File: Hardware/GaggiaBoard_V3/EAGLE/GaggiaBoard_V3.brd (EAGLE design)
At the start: 45 x 100 mm, 68 parts, among them IC1 LD117AS33TR, J1 4PIN, J10 PIN262409-1, J11 PIN262409-1, J12 PIN262409-1, J13 PIN262409-1, J2 Vertical Qwiic Connector, J5 2PIN, J6 3PIN, J7 3PIN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

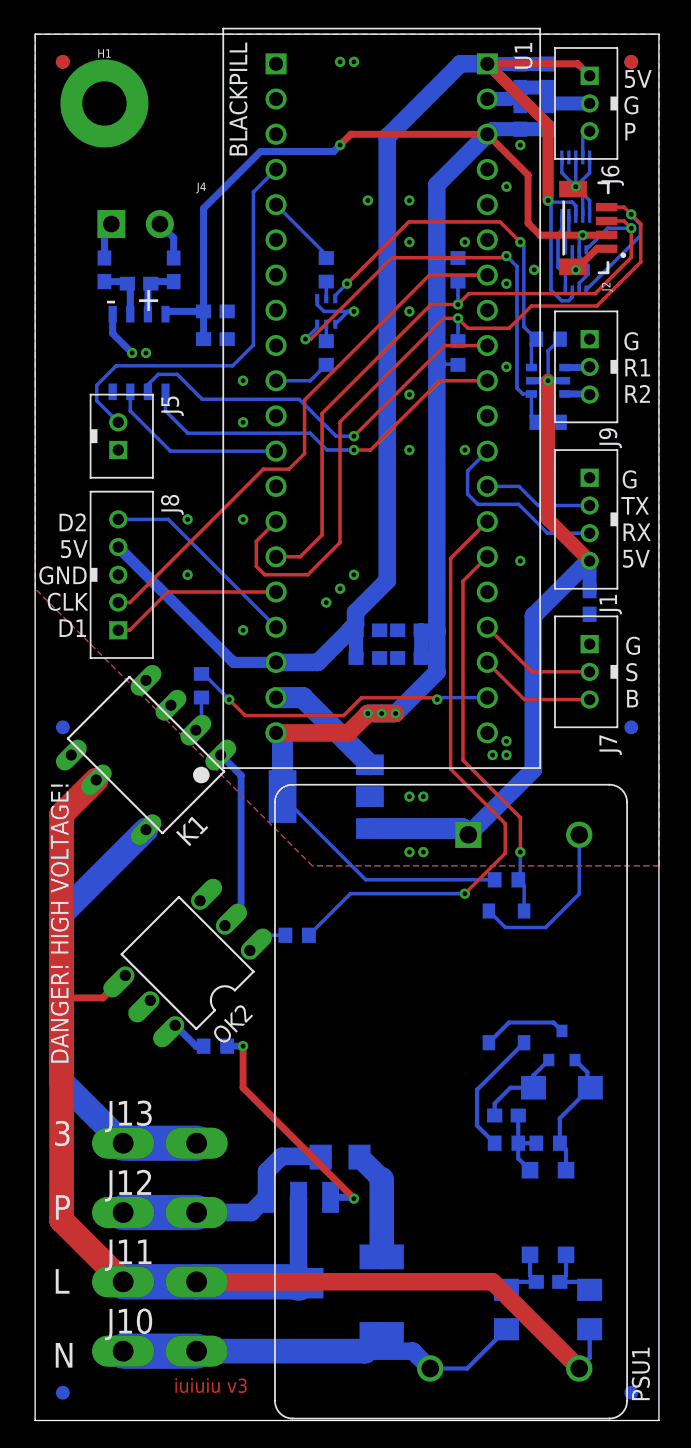
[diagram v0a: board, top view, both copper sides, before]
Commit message: UART added
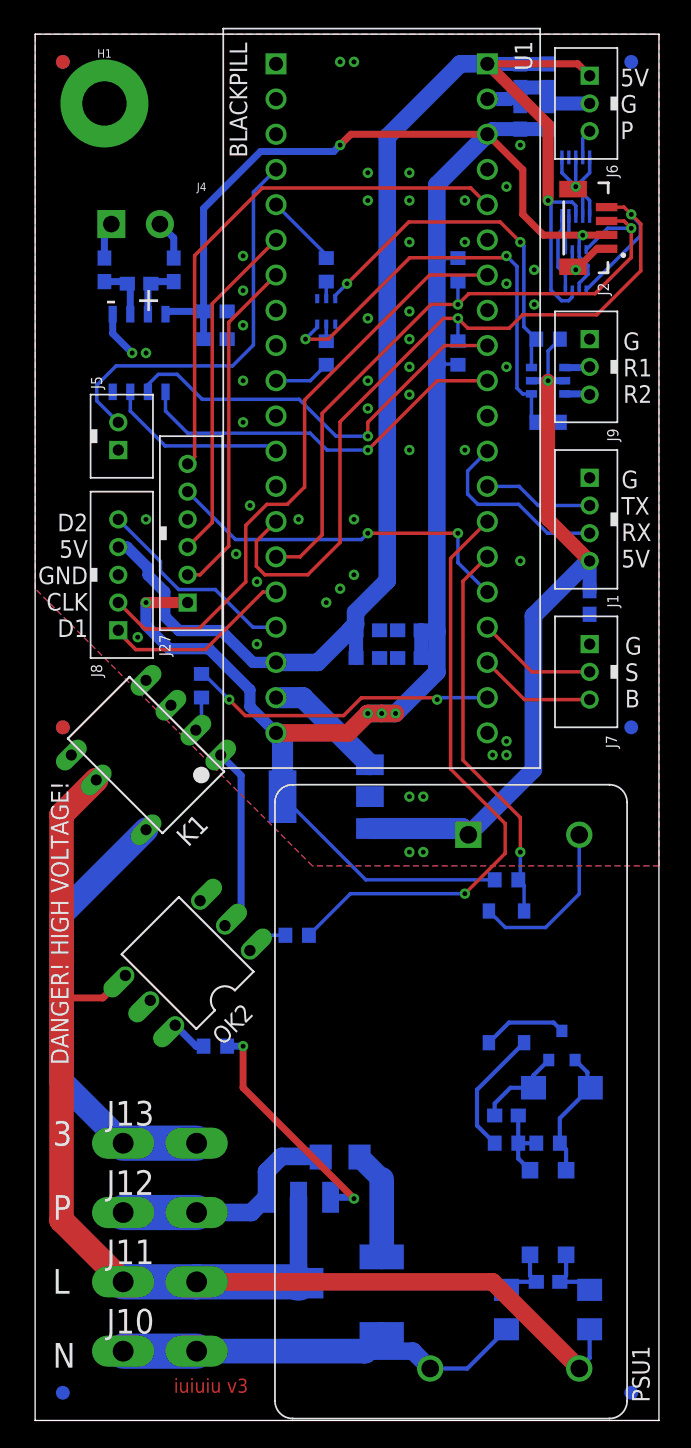
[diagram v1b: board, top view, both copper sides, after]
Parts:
- added J27: 6PIN, jst_eph:B6B-PH-K-S
- moved MARK8 63.1 mm to (2.00, 50.0)
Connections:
- net 3V3: now also J27.1
- net BOOT1: now also J27.6
- net GND: now also J27.4
- net NRST: now also J27.5
- net UART1_RX: now also J27.2
- net UART1_TX: now also J27.3
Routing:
- net BOOT1: track 0.00 -> 38.9 mm
- net NRST: track 0.00 -> 26.2 mm, vias 0 -> 2
- net UART1_TX: track 0.00 -> 24.8 mm
- net UART1_RX: track 0.00 -> 24.8 mm
- net 3V3: track 142.3 -> 160.1 mm, vias 5 -> 6
- net PB0: track 38.7 -> 44.0 mm
- net GND: track 69.7 -> 64.6 mm, vias 37 -> 52
- net 5V: track 161.6 -> 163.0 mm
- net PB8: track 12.5 -> 13.8 mm
- net PA6: track 29.9 -> 30.4 mm
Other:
- board text added: "BOOT1 NRST GND TX RX 3V3"

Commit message: README + PC13 load fix
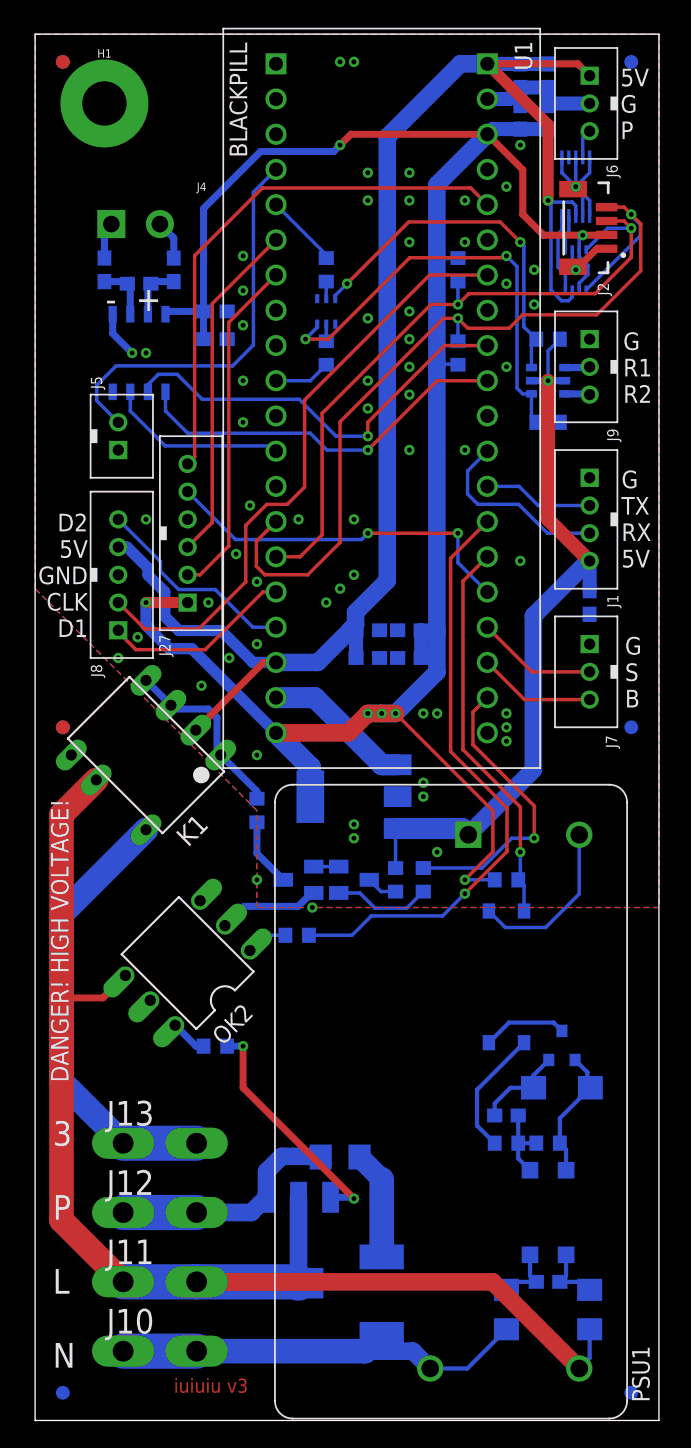
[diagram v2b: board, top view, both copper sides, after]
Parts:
- added R3, R4: 10K, rcl:R0603
- added T1, T2: (no value), transistor:SOT23-BEC
- R8: value 10K -> 220
- moved R8 9.85 mm to (16.0, 44.0), turned to 90 degrees
- moved IC1 2.00 mm to (23.0, 45.0)
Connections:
- new net N$11: R8.1, T2.C
- new net N$12: T1.E, T2.B
- new net N$13: K1.1, K1.3, K1.4, R8.2
- new net N$14: R4.2, T1.B
- net 5V: now also K1.2, R3.2
- net GND: now also T2.E; no longer K1.1, K1.3, K1.4
- net N$1: now also R3.1, T1.C; no longer K1.2, R8.2
- net PC13: now also R4.1; no longer R8.1
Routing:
- net N$13: track 0.00 -> 13.3 mm
- net 5V: track 163.0 -> 171.7 mm
- net N$14: track 0.00 -> 7.05 mm
- net N$11: track 0.00 -> 4.94 mm
- net GND: track 64.6 -> 60.6 mm, vias 52 -> 62
- net N$12: track 0.00 -> 1.80 mm
- net PC13: track 22.5 -> 21.3 mm, vias 2 -> 1
- net 3V3: track 160.1 -> 160.3 mm, vias 6 -> 7

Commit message: J1 fix
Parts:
- moved C4 9.49 mm to (37.0, 68.0), turned to 0 degrees
- moved FB2 2.50 mm to (3.50, 85.0)
- moved FB1 2.24 mm to (11.0, 85.0)
- moved C1 2.00 mm to (13.0, 82.0)
- moved C2 2.00 mm to (13.0, 80.0)
- moved C3 2.00 mm to (7.50, 84.0)
- moved U2 2.00 mm to (7.50, 79.0)
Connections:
- net 5V: now also J1.1; no longer J1.4
- net GND: now also J1.4; no longer J1.1
- net UART2_RX: now also J1.2; no longer J1.3
- net UART2_TX: now also J1.3; no longer J1.2
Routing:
- net UART2_RX: track 13.7 -> 9.00 mm
- net SPI1_SCK: track 27.8 -> 29.8 mm
- net SPI1_MISO: track 13.1 -> 15.1 mm
- net 3V3: track 160.3 -> 158.3 mm
- net N$5: track 4.00 -> 5.50 mm
- net N$26: track 4.00 -> 5.00 mm
- net 5V: track 171.7 -> 172.6 mm
- net UART2_TX: track 7.95 -> 8.78 mm
- net PB15: track 29.2 -> 30.0 mm
- net PA6: track 30.4 -> 31.2 mm
- net N$4: track 2.86 -> 2.19 mm
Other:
- board text added: "5V RX TX G"
- board text removed: "G TX RX 5V"

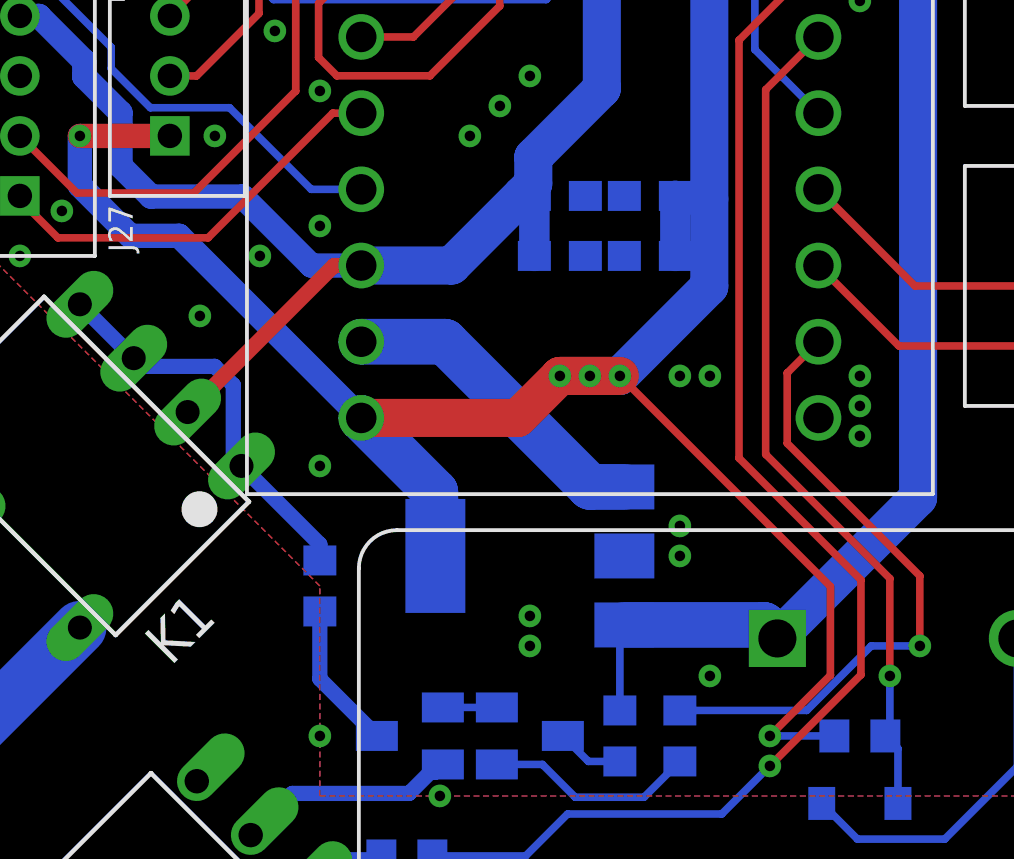
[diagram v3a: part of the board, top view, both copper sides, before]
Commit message: 5V supply fix
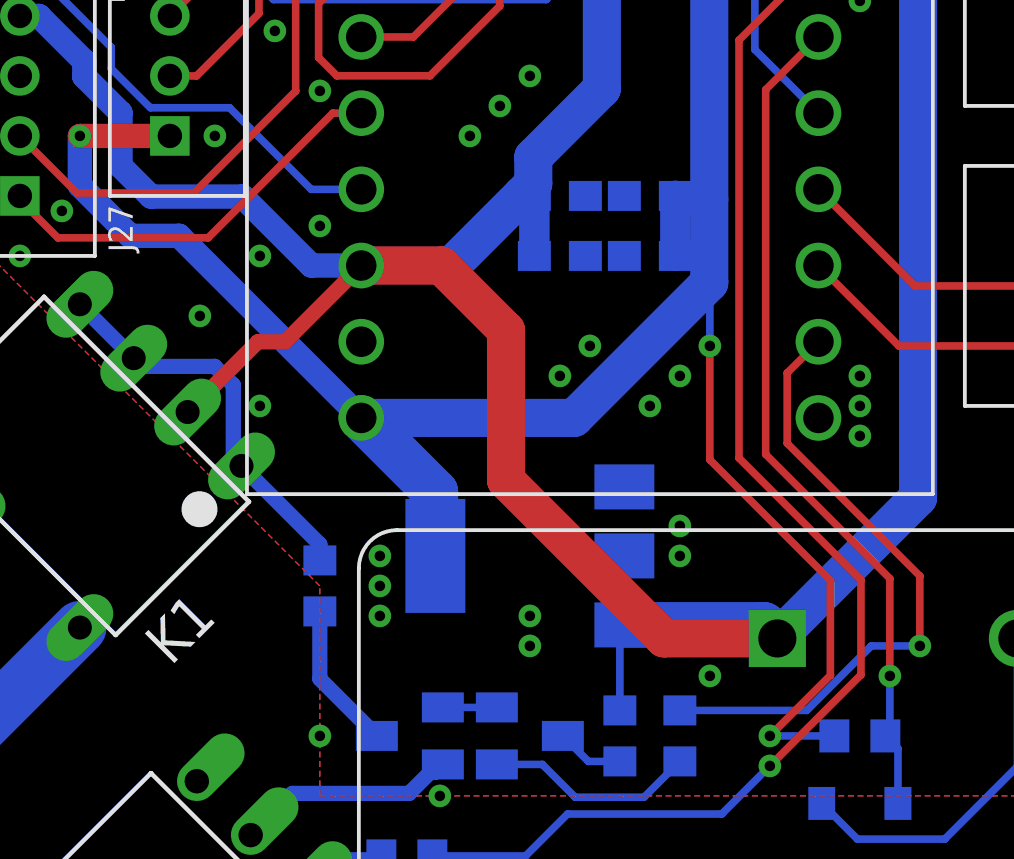
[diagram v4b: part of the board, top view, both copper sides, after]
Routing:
- net 5V: track 172.6 -> 194.6 mm
- net GND: track 60.6 -> 49.9 mm, vias 62 -> 67
- net 3V3: track 158.3 -> 158.1 mm, vias 7 -> 5
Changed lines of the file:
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@@
 <setting verticaltext="up"/>
 </settings>
-<grid distance="50" unitdist="mil" unit="mil" style="lines" multiple="1" display="no" altdistance="5" altunitdist="mil" altunit="mil"/>
+<grid distance="1" unitdist="mm" unit="mm" style="lines" multiple="1" display="no" altdistance="0.1" altunitdist="mm" altunit="mm"/>
 <layers>
 <layer number="1" name="Top" color="4" fill="1" visible="yes" active="yes"/>
@@
 <element name="T2" library="transistor" library_urn="urn:adsk.eagle:library:402" package="SOT23-BEC" package3d_urn="urn:adsk.eagle:package:28748/2" value="" x="19" y="39" smashed="yes" rot="MR270">
 <attribute name="LCSC" value="C82460" x="19" y="39" size="1.778" layer="28" rot="MR270" display="off"/>
-<attribute name="NAME" x="17.995" y="42.505" size="1.27" layer="26" rot="MR270"/>
+<attribute name="NAME" x="17.795" y="42.205" size="1.27" layer="26" rot="MR270"/>
 <attribute name="POPULARITY" value="0" x="19" y="39" size="1.778" layer="28" rot="MR270" display="off"/>
 <attribute name="VALUE" x="22.175" y="40.905" size="1.27" layer="28" rot="MR270"/>
@@
 <wire x1="38.75" y1="84.45" x2="38.75" y2="83.25" width="0.254" layer="16"/>
 <wire x1="38.75" y1="83.25" x2="39" y2="83" width="0.254" layer="16"/>
-<wire x1="17.38" y1="52.14" x2="20.167" y2="52.14" width="1.524" layer="16"/>
-<wire x1="25.007" y1="47.3" x2="20.167" y2="52.14" width="1.524" layer="16"/>
-<wire x1="25.007" y1="47.3" x2="26.15" y2="47.3" width="1.524" layer="16"/>
 <via x="7" y="79" extent="1-16" drill="0.35"/>
 <via x="8" y="79" extent="1-16" drill="0.35"/>
@@
 <via x="12" y="53" extent="1-16" drill="0.35"/>
 <via x="14" y="55" extent="1-16" drill="0.35"/>
-<via x="16" y="48" extent="1-16" drill="0.35"/>
+<via x="14" y="50" extent="1-16" drill="0.35"/>
 <via x="16" y="39" extent="1-16" drill="0.35"/>
 <via x="20" y="37" extent="1-16" drill="0.35"/>
 <via x="29" y="41" extent="1-16" drill="0.35"/>
-<via x="29" y="51" extent="1-16" drill="0.35"/>
+<via x="27" y="50" extent="1-16" drill="0.35"/>
 <via x="28" y="51" extent="1-16" drill="0.35"/>
 <via x="12.5" y="59" extent="1-16" drill="0.35"/>
 <contactref element="J1" pad="4"/>
+<via x="18" y="45" extent="1-16" drill="0.35"/>
+<via x="25" y="52" extent="1-16" drill="0.35"/>
+<via x="24" y="51" extent="1-16" drill="0.35"/>
+<via x="18" y="44" extent="1-16" drill="0.35"/>
+<via x="18" y="43" extent="1-16" drill="0.35"/>
 </signal>
 <signal name="5V">
@@
 <wire x1="26" y1="39.85" x2="26" y2="42.55" width="0.254" layer="16"/>
 <wire x1="26" y1="42.55" x2="26.15" y2="42.7" width="0.254" layer="16"/>
-<wire x1="11.5921" y1="49.79605" x2="16.47605" y2="54.68" width="0.508" layer="1"/>
-<wire x1="16.47605" y1="54.68" x2="17.38" y2="54.68" width="0.508" layer="1"/>
+<wire x1="11.5921" y1="49.79605" x2="13.93605" y2="52.14" width="0.508" layer="1"/>
+<wire x1="14.84" y1="52.14" x2="13.93605" y2="52.14" width="0.508" layer="1"/>
+<wire x1="14.84" y1="52.14" x2="17.38" y2="54.68" width="0.508" layer="1"/>
 <contactref element="J1" pad="1"/>
 <wire x1="40" y1="68" x2="38.85" y2="68" width="1.016" layer="1"/>
@@
 <wire x1="40" y1="68" x2="39.365" y2="68" width="1.016" layer="16"/>
 <wire x1="39.365" y1="68" x2="35.941" y2="64.576" width="1.016" layer="16"/>
-<wire x1="38.75" y1="81.55" x2="37.85" y2="78" width="0" layer="19" extent="16-16"/>
+<wire x1="17.38" y1="54.68" x2="20.047" y2="54.68" width="1.27" layer="1"/>
+<wire x1="22.206" y1="52.521" x2="20.047" y2="54.68" width="1.27" layer="1"/>
+<wire x1="22.206" y1="52.521" x2="22.206" y2="47.517" width="1.27" layer="1"/>
+<wire x1="31.25" y1="42.25" x2="27.473" y2="42.25" width="1.27" layer="1"/>
+<wire x1="27.473" y1="42.25" x2="22.206" y2="47.517" width="1.27" layer="1"/>
 </signal>
 <signal name="3V3">
@@
 <wire x1="39.878" y1="83.312" x2="39.878" y2="82.677" width="0.254" layer="16"/>
 <wire x1="39.878" y1="82.677" x2="39.25" y2="82.049" width="0.254" layer="16"/>
-<via x="24" y="51" extent="1-16" drill="0.35"/>
-<via x="25" y="51" extent="1-16" drill="0.35"/>
-<via x="26" y="51" extent="1-16" drill="0.35"/>
+<via x="29" y="52" extent="1-16" drill="0.35"/>
 <wire x1="32.62" y1="92.78" x2="28.9814" y2="89.1414" width="1.27" layer="16"/>
 <wire x1="28.9814" y1="89.1414" x2="28.9814" y2="83.82" width="1.27" layer="16"/>
 <wire x1="28.9814" y1="83.82" x2="28.9814" y2="76.2" width="1.27" layer="16"/>
 <wire x1="28.9814" y1="76.2" x2="28.9814" y2="56.896" width="1.27" layer="16"/>
-<wire x1="28.9814" y1="56.896" x2="28.9814" y2="53.9814" width="1.27" layer="16"/>
-<wire x1="28.9814" y1="53.9814" x2="26" y2="51" width="1.27" layer="16"/>
-<wire x1="25" y1="51" x2="26" y2="51" width="1.27" layer="16"/>
-<wire x1="24" y1="51" x2="25" y2="51" width="1.27" layer="16"/>
-<wire x1="17.38" y1="49.6" x2="22.6" y2="49.6" width="1.27" layer="1"/>
-<wire x1="22.6" y1="49.6" x2="24" y2="51" width="1.27" layer="1"/>
-<wire x1="25" y1="51" x2="24" y2="51" width="1.27" layer="1"/>
-<wire x1="26" y1="51" x2="25" y2="51" width="1.27" layer="1"/>
+<wire x1="28.9814" y1="56.896" x2="28.9814" y2="54.1084" width="1.27" layer="16"/>
 <wire x1="27.85" y1="55" x2="27.85" y2="57" width="1.016" layer="16"/>
 <wire x1="27.85" y1="57" x2="27.954" y2="56.896" width="1.016" layer="16"/>
@@
 <via x="31" y="39" extent="1-16" drill="0.35"/>
 <wire x1="31" y1="39" x2="33.02" y2="41.02" width="0.254" layer="1"/>
-<wire x1="33.02" y1="43.98" x2="26" y2="51" width="0.254" layer="1"/>
-<wire x1="33.02" y1="41.02" x2="33.02" y2="43.98" width="0.254" layer="1"/>
+<wire x1="33.02" y1="44.186" x2="29" y2="48.206" width="0.254" layer="1"/>
+<wire x1="29" y1="48.206" x2="29" y2="52" width="0.254" layer="1"/>
+<wire x1="33.02" y1="41.02" x2="33.02" y2="44.186" width="0.254" layer="1"/>
+<wire x1="17.38" y1="49.6" x2="24.473" y2="49.6" width="1.27" layer="16"/>
+<wire x1="24.473" y1="49.6" x2="28.9814" y2="54.1084" width="1.27" layer="16"/>
+<wire x1="29" y1="52" x2="29" y2="54.0898" width="0.254" layer="16"/>
+<wire x1="29" y1="54.0898" x2="28.9814" y2="54.1084" width="0.254" layer="16"/>
 </signal>
 <signal name="I2C2_SDA">

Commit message: snubbers
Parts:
- added C16: 10nF, rcl:C1206
- added R5: 220, rcl:R2512
- moved R13 12.5 mm to (19.0, 20.0), turned to 0 degrees
- moved C5 6.71 mm to (25.0, 13.0), turned to 90 degrees
- moved R2 3.16 mm to (10.0, 26.0)
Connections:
- removed net N$32: C5.1, R13.2
- new net N$15: C16.2, R5.1
- new net N$16: C5.2, R13.1
- net 3WAY: now also R5.2
- net AC_N: no longer R13.1
- net AC_P: now also C16.1, C5.1
- net PUMP_P: now also R13.2; no longer C5.2
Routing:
- net AC_N: track 43.2 -> 29.3 mm
- net N$15: track 0.00 -> 13.2 mm
- net AC_P: track 96.5 -> 106.3 mm
- net N$32: track 7.86 -> 0.00 mm
- net 3WAY: track 32.3 -> 39.3 mm
- net N$16: track 0.00 -> 6.93 mm
- net GND: track 49.9 -> 54.1 mm
- net PUMP_P: track 17.0 -> 20.0 mm
- net N$9: track 17.2 -> 19.7 mm
